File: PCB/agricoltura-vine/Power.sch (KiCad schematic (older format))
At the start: 22 parts, among them T16 0395121002, U4 AP63203WU-7, U5 AP63205WU-7

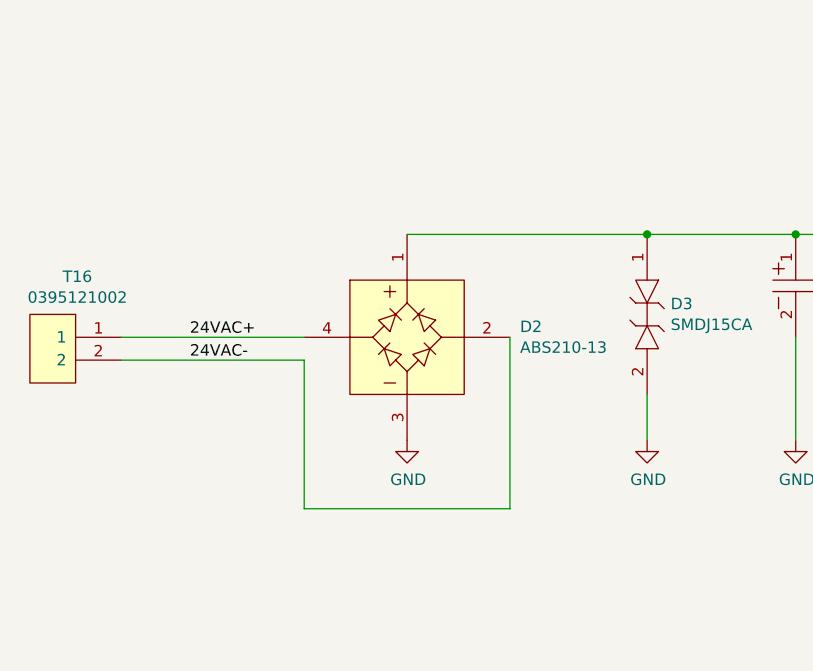
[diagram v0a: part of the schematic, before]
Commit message: DC Power
Power input section converted to 24VDC Max input instead of AC. A proper AC to DC power supply would need more components to be properly implmented and not require redesign of the DCDC regulators. Also the plan going forward is to be able to run thes off rechargeable battery packs as well as 24VDC bus voltages.
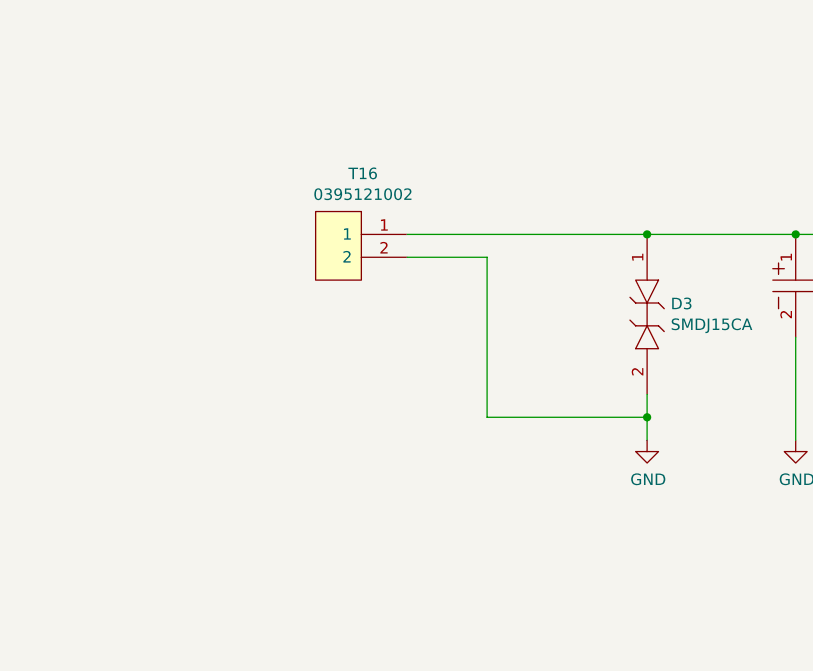
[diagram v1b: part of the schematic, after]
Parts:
- removed D2: ABS210-13, AVR-KiCAD-Lib-Diodes:ABS210-13, symbol AVR-KiCAD-Lib-Diodes:ABS210-13
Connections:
- net 24VAC+ is gone; now on net +24V: T16.1
- net 24VAC- is gone; now on net GND: T16.2
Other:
- moved on the sheet: T16
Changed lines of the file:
@@
 Comment4 ""
 $EndDescr
-$Comp
-L AVR-KiCAD-Lib-Diodes:ABS210-13 D2
-U 1 1 5EEC167B
-P 2400 3250
-F 0 "D2" H 3144 3046 50  0000 L CNN
-F 1 "ABS210-13" H 2650 4100 50  0001 C CNN
-F 2 "AVR-KiCAD-Lib-Diodes:ABS210-13" V 2800 3150 50  0001 C CNN
-F 3 "https://www.comchiptech.com/admin/files/product/20190215095655.pdf" H 2400 3300 50  0001 C CNN
-F 4 "0.45000" H 2700 4150 50  0001 C CNN "Cost QTY: 1"
-F 5 "0.10988" H 2800 4250 50  0001 C CNN "Cost QTY: 1000"
-F 6 "0.10054" H 2900 4350 50  0001 C CNN "Cost QTY: 2500"
-F 7 "0.09615" H 3000 4450 50  0001 C CNN "Cost QTY: 5000"
-F 8 "0.08516" H 3100 4550 50  0001 C CNN "Cost QTY: 10000"
-F 9 "Diodes Incorporated" H 3200 4650 50  0001 C CNN "MFR"
-F 10 "ABS210-13" H 3300 4750 50  0001 C CNN "MFR#"
-F 11 "Digikey" H 3400 4850 50  0001 C CNN "Vendor"
-F 12 "ABS210-13DICT-ND" H 3500 4950 50  0001 C CNN "Vendor #"
-F 13 "AVR" H 3600 5050 50  0001 C CNN "Designer"
-F 14 "2.6mm" H 3700 5150 50  0001 C CNN "Height"
-F 15 "3/23/2020" H 4800 6250 50  0001 C CNN "Date Created"
-F 16 "4/12/2020" H 3800 5250 50  0001 C CNN "Date Modified"
-F 17 "Yes" H 3900 5350 50  0001 C CNN "Lead-Free ?"
-F 18 "1" H 4000 5450 50  0001 C CNN "RoHS Levels"
-F 19 "SMT" H 4100 5550 50  0001 C CNN "Mounting"
-F 20 "4" H 4200 5650 50  0001 C CNN "Pin Count #"
-F 21 "Active" H 4300 5750 50  0001 C CNN "Status"
-F 22 "*" H 4400 5850 50  0001 C CNN "Tolerance"
-F 23 "Rectifier Diode" H 4500 5950 50  0001 C CNN "Type"
-F 24 "1KV 2A" H 4600 6050 50  0001 C CNN "Voltage"
-F 25 "4-SOPA" H 4700 6200 50  0001 C CNN "Package"
-F 26 "Bridge Rectifier Single Phase Standard 1kV Surface Mount 4-SOPA" H 5000 6500 50  0001 C CNN "Description"
-F 27 "ABS210-13" H 3144 2955 50  0000 L CNN "_Value_"
-F 28 "*" H 5000 6500 50  0001 C CNN "Management_ID"
-	1    2400 3250
-	1    0    0    -1
-$EndComp
-Wire Wire Line
-	1400 3600 2200 3600
-Wire Wire Line
-	2200 3600 2200 4250
-Wire Wire Line
-	2200 4250 3100 4250
-Wire Wire Line
-	3100 4250 3100 3500
-$Comp
-L power:GND #PWR028
-U 1 1 5EEC4A33
-P 2650 3950
-F 0 "#PWR028" H 2650 3700 50  0001 C CNN
-F 1 "GND" H 2655 3777 50  0000 C CNN
-F 2 "" H 2650 3950 50  0001 C CNN
-F 3 "" H 2650 3950 50  0001 C CNN
-	1    2650 3950
-	1    0    0    -1
-$EndComp
 Wire Wire Line
 	2650 3050 3700 3050
@@
 $EndComp
 Wire Wire Line
-	3700 3950 3700 3750
+	3700 3950 3700 3850
 $Comp
 L power:+24V #PWR031
@@
 Wire Wire Line
 	2550 6200 2550 6500
-Wire Wire Line
-	1400 3500 2200 3500
-Text Label 1700 3500 0    50   ~ 0
-24VAC+
-Text Label 1700 3600 0    50   ~ 0
-24VAC-
 $Comp
 L power:Earth #PWR0114
@@
 L AVR-KiCAD-Lib-Connectors:0395121002 T16
 U 1 1 5F06CA83
-P 1200 3500
-F 0 "T16" H 1192 3765 50  0000 C CNN
-F 1 "0395121002" H 1192 3674 50  0000 C CNN
-F 2 "AVR-KiCAD-Lib-Connectors:0395121002" H 250 4550 50  0001 C CNN
-F 3 "https://www.molex.com/pdm_docs/sd/395121002_sd.pdf" H 1100 3600 50  0001 C CNN
-F 4 "0.90000" H 1300 3750 50  0001 C CNN "Cost QTY: 1"
-F 5 "0.30600" H 1400 3850 50  0001 C CNN "Cost QTY: 1000"
-F 6 "*" H 1500 3950 50  0001 C CNN "Cost QTY: 2500"
-F 7 "0.23940" H 1600 4050 50  0001 C CNN "Cost QTY: 5000"
-F 8 "*" H 1700 4150 50  0001 C CNN "Cost QTY: 10000"
-F 9 "Molex" H 1800 4250 50  0001 C CNN "MFR"
-F 10 "0395121002" H 1900 4350 50  0001 C CNN "MFR#"
-F 11 "Digikey" H 2000 4450 50  0001 C CNN "Vendor"
-F 12 "WM23198-ND" H 2100 4550 50  0001 C CNN "Vendor #"
-F 13 "AVR" H 2200 4650 50  0001 C CNN "Designer"
-F 14 "6.86mm" H 2300 4750 50  0001 C CNN "Height"
-F 15 "6/23/2020" H 3400 5850 50  0001 C CNN "Date Created"
-F 16 "6/23/2020" H 2400 4850 50  0001 C CNN "Date Modified"
-F 17 "Yes" H 2500 4950 50  0001 C CNN "Lead-Free ?"
-F 18 "1" H 2600 5050 50  0001 C CNN "RoHS Levels"
-F 19 "ThroughHole" H 2700 5150 50  0001 C CNN "Mounting"
-F 20 "2" H 2800 5250 50  0001 C CNN "Pin Count #"
-F 21 "Active" H 2900 5350 50  0001 C CNN "Status"
-F 22 "*" H 3000 5450 50  0001 C CNN "Tolerance"
-F 23 "Connector" H 3100 5550 50  0001 C CNN "Type"
-F 24 "300V" H 3200 5650 50  0001 C CNN "Voltage"
-F 25 "*" H 3300 5800 50  0001 C CNN "Package"
-F 26 "2 Position Terminal Block Header, Male Pins, Shrouded (4 Side) 0.150\" (3.81mm) 90°, Right Angle  Through Hole" H 3700 6200 50  0001 C CNN "Description"
-F 27 "0395121002" H 3500 6000 50  0001 C CNN "_Value_"
-F 28 "*" H 3600 6100 50  0001 C CNN "Management_ID"
-	1    1200 3500
+P 2450 3050
+F 0 "T16" H 2442 3315 50  0000 C CNN
+F 1 "0395121002" H 2442 3224 50  0000 C CNN
+F 2 "AVR-KiCAD-Lib-Connectors:0395121002" H 1500 4100 50  0001 C CNN
+F 3 "https://www.molex.com/pdm_docs/sd/395121002_sd.pdf" H 2350 3150 50  0001 C CNN
+F 4 "0.90000" H 2550 3300 50  0001 C CNN "Cost QTY: 1"
+F 5 "0.30600" H 2650 3400 50  0001 C CNN "Cost QTY: 1000"
+F 6 "*" H 2750 3500 50  0001 C CNN "Cost QTY: 2500"
+F 7 "0.23940" H 2850 3600 50  0001 C CNN "Cost QTY: 5000"
+F 8 "*" H 2950 3700 50  0001 C CNN "Cost QTY: 10000"
+F 9 "Molex" H 3050 3800 50  0001 C CNN "MFR"
+F 10 "0395121002" H 3150 3900 50  0001 C CNN "MFR#"
+F 11 "Digikey" H 3250 4000 50  0001 C CNN "Vendor"
+F 12 "WM23198-ND" H 3350 4100 50  0001 C CNN "Vendor #"
+F 13 "AVR" H 3450 4200 50  0001 C CNN "Designer"
+F 14 "6.86mm" H 3550 4300 50  0001 C CNN "Height"
+F 15 "6/23/2020" H 4650 5400 50  0001 C CNN "Date Created"
+F 16 "6/23/2020" H 3650 4400 50  0001 C CNN "Date Modified"
+F 17 "Yes" H 3750 4500 50  0001 C CNN "Lead-Free ?"
+F 18 "1" H 3850 4600 50  0001 C CNN "RoHS Levels"
+F 19 "ThroughHole" H 3950 4700 50  0001 C CNN "Mounting"
+F 20 "2" H 4050 4800 50  0001 C CNN "Pin Count #"
+F 21 "Active" H 4150 4900 50  0001 C CNN "Status"
+F 22 "*" H 4250 5000 50  0001 C CNN "Tolerance"
+F 23 "Connector" H 4350 5100 50  0001 C CNN "Type"
+F 24 "300V" H 4450 5200 50  0001 C CNN "Voltage"
+F 25 "*" H 4550 5350 50  0001 C CNN "Package"
+F 26 "2 Position Terminal Block Header, Male Pins, Shrouded (4 Side) 0.150\" (3.81mm) 90°, Right Angle  Through Hole" H 4950 5750 50  0001 C CNN "Description"
+F 27 "0395121002" H 4750 5550 50  0001 C CNN "_Value_"
+F 28 "*" H 4850 5650 50  0001 C CNN "Management_ID"
+	1    2450 3050
 	-1   0    0    -1
 $EndComp
+Wire Wire Line
+	2650 3150 3000 3150
+Wire Wire Line
+	3000 3150 3000 3850
+Wire Wire Line
+	3000 3850 3700 3850
+Connection ~ 3700 3850
+Wire Wire Line
+	3700 3850 3700 3750
 $EndSCHEMATC
